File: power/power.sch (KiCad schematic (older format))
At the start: 83 parts, among them J1 Conn_01x02_Female, J2 Conn_01x02_Female, J3 CONN_02X03, J4 Conn_01x06_Female, Q1 BS170, Q10 BS170, Q11 BS170, Q12 BSB014N04LX3, Q2 BS170, Q3 BS170, Q4 BS170, Q5 BS170, Q6 BS170, Q7 BS170, Q8 BS170, Q9 BS170, U1 MAX1648, U2 TPS2592xx, U3 LMC6482

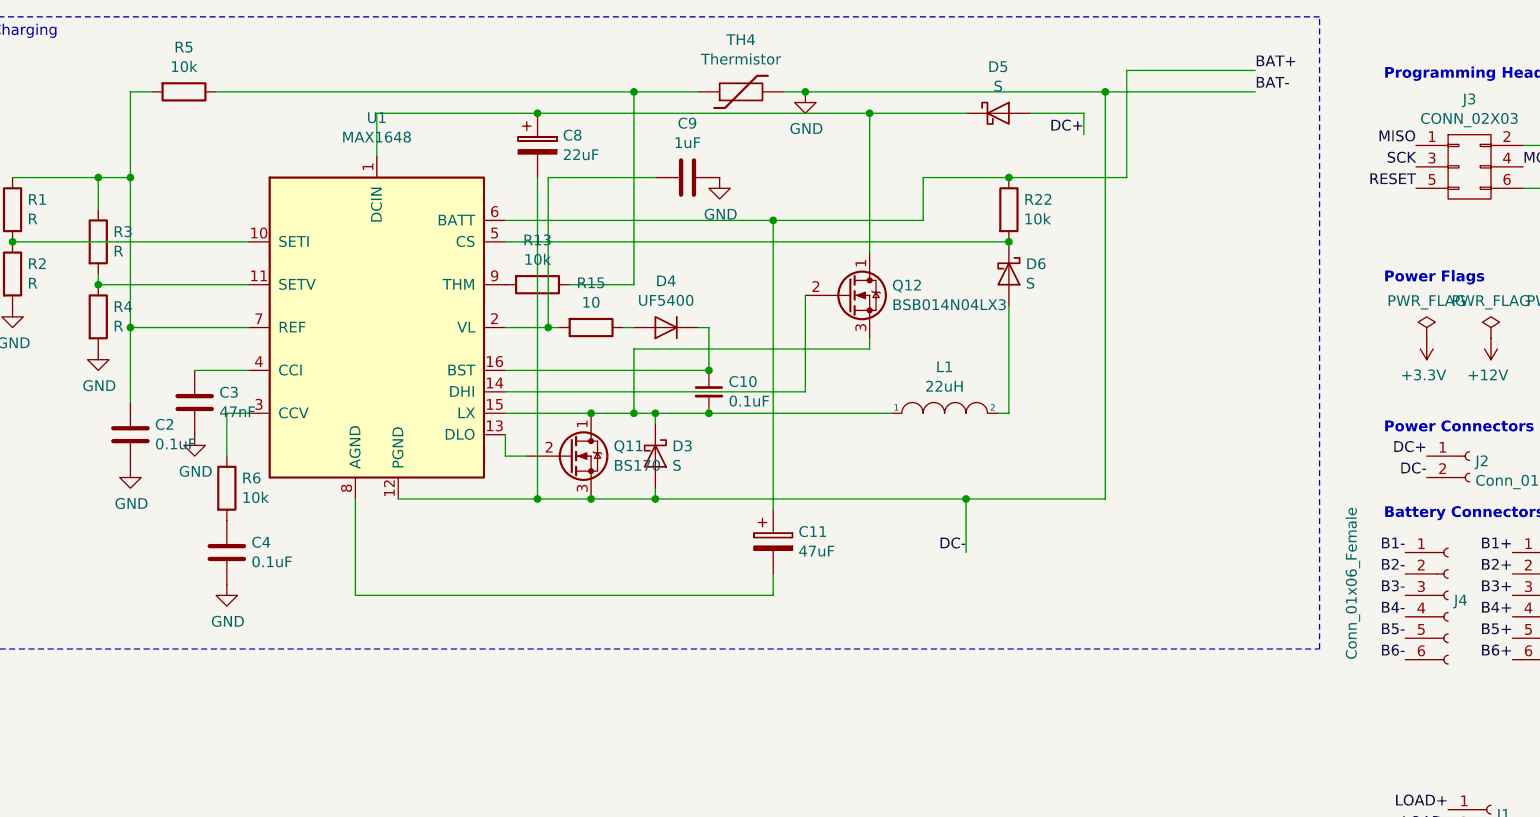
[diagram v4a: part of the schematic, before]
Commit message: wattage and values for charging circuit
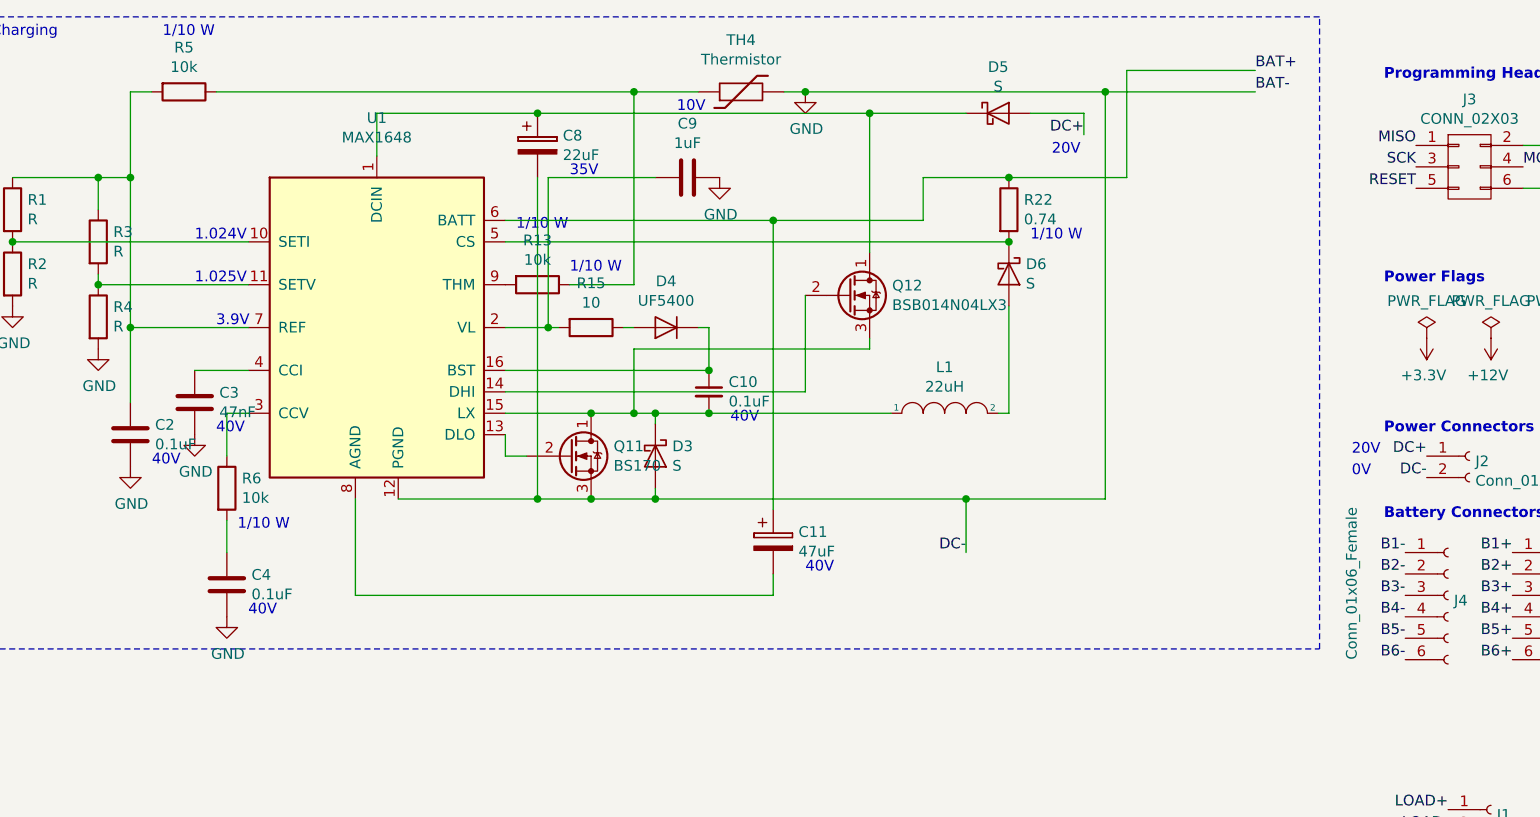
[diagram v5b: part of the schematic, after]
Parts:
- R22: value 10k -> 0.74
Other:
- note added: "0V"
- note added: "1.024V"
- note added: "1.025V"
- note added: "1/10 W"
- note added: "10V"
- note added: "20V"
- note added: "3.9V"
- note added: "35V"
- note added: "40V"
- moved on the sheet: C4
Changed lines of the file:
@@
 P 5300 1400
 F 0 "R22" H 5370 1446 50  0000 L CNN
-F 1 "10k" H 5370 1355 50  0000 L CNN
+F 1 "0.74" H 5370 1355 50  0000 L CNN
 F 2 "Resistor_SMD:R_0805_2012Metric_Pad1.15x1.40mm_HandSolder" V 5230 1400 50  0001 C CNN
 F 3 "~" H 5300 1400 50  0001 C CNN
@@
 L Device:C C4
 U 1 1 5E57A175
-P 1650 3000
-F 0 "C4" H 1535 2954 50  0000 R CNN
-F 1 "0.1uF" H 1535 3045 50  0000 R CNN
-F 2 "Capacitor_SMD:C_0805_2012Metric_Pad1.15x1.40mm_HandSolder" H 1688 2850 50  0001 C CNN
-F 3 "~" H 1650 3000 50  0001 C CNN
-	1    1650 3000
+P 1650 3150
+F 0 "C4" H 1535 3104 50  0000 R CNN
+F 1 "0.1uF" H 1535 3195 50  0000 R CNN
+F 2 "Capacitor_SMD:C_0805_2012Metric_Pad1.15x1.40mm_HandSolder" H 1688 3000 50  0001 C CNN
+F 3 "~" H 1650 3150 50  0001 C CNN
+	1    1650 3150
 	-1   0    0    1
 $EndComp
@@
 L power:GND #PWR0111
 U 1 1 5E588124
-P 1650 3150
-F 0 "#PWR0111" H 1650 2900 50  0001 C CNN
-F 1 "GND" H 1655 2977 50  0000 C CNN
-F 2 "" H 1650 3150 50  0001 C CNN
-F 3 "" H 1650 3150 50  0001 C CNN
-	1    1650 3150
+P 1650 3300
+F 0 "#PWR0111" H 1650 3050 50  0001 C CNN
+F 1 "GND" H 1655 3127 50  0000 C CNN
+F 2 "" H 1650 3300 50  0001 C CNN
+F 3 "" H 1650 3300 50  0001 C CNN
+	1    1650 3300
 	1    0    0    -1
 $EndComp
@@
 Text Label 10600 2500 0    50   ~ 0
 SafetySwitchB
+Text Notes 1700 2900 0    50   ~ 0
+1/10 W
+Wire Wire Line
+	1650 2850 1650 3000
+Text Notes 1750 3300 0    50   ~ 0
+40V
+Text Notes 1350 600  0    50   ~ 0
+1/10 W
+Text Notes 3000 1500 0    50   ~ 0
+1/10 W
+Text Notes 3250 1700 0    50   ~ 0
+1/10 W
+Text Notes 4350 3100 0    50   ~ 0
+40V
+Text Notes 4000 2400 0    50   ~ 0
+40V
+Text Notes 3250 1250 0    50   ~ 0
+35V
+Text Notes 3750 950  0    50   ~ 0
+10V
+Text Notes 1300 2600 0    50   ~ 0
+40V
+Text Notes 1600 2450 0    50   ~ 0
+40V
+Text Notes 5500 1150 0    50   ~ 0
+20V
+Text Notes 6900 2550 0    50   ~ 0
+20V
+Text Notes 6900 2650 0    50   ~ 0
+0V
+Text Notes 1600 1950 0    50   ~ 0
+3.9V
+Text Notes 1500 1550 0    50   ~ 0
+1.024V
+Text Notes 5400 1550 0    50   ~ 0
+1/10 W
+Text Notes 1500 1750 0    50   ~ 0
+1.025V
 $EndSCHEMATC

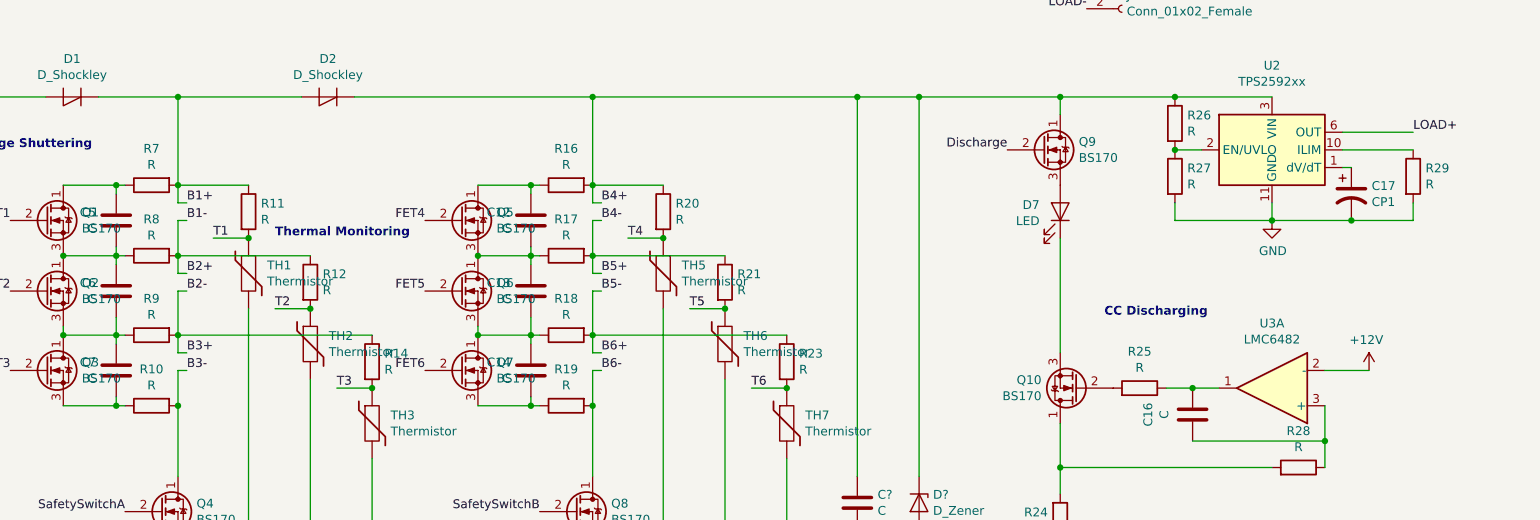
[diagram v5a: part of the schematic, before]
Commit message: bleeding resistor values and wattage, discharging current sink circuit complete
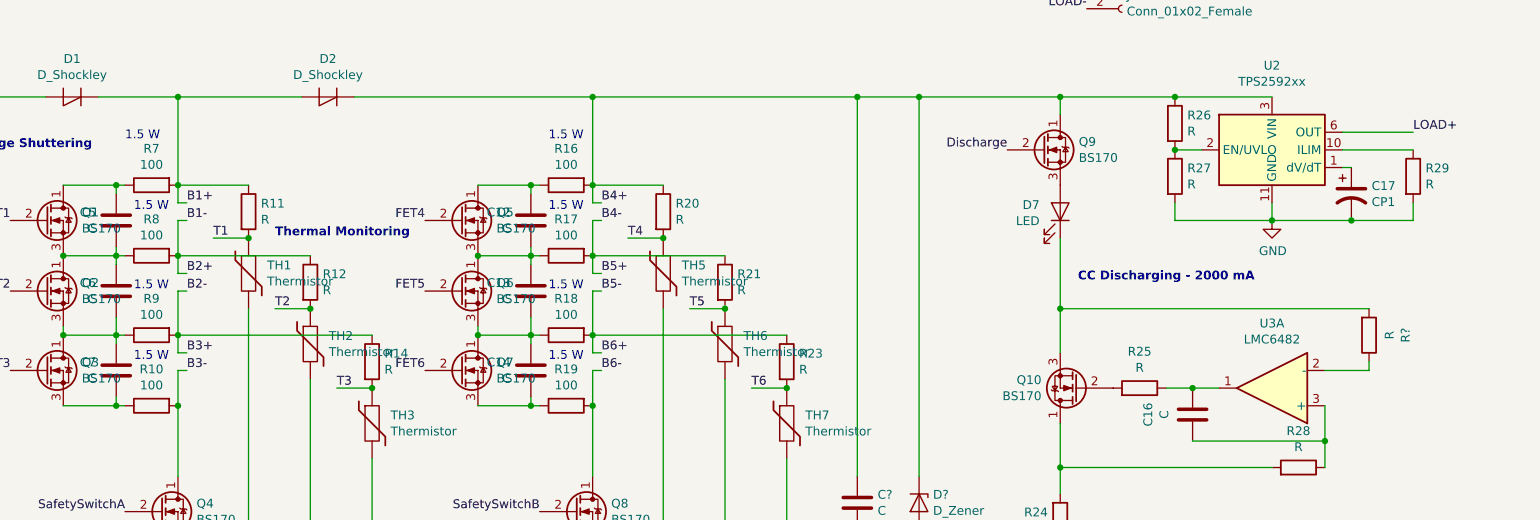
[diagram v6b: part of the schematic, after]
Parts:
- added R?: R, Resistor_SMD:R_0805_2012Metric_Pad1.15x1.40mm_HandSolder, symbol Device:R
- R10, R16, R17, R18, R19, R7, R8, R9: value R -> 100
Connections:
- net +12V: no longer U3.2 (-)
- net at D7.1 (K), Q10.3 (S): now also R?.2
- new net: R?.1, U3.2 (-)
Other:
- note added: "1.5 W"
- note added: "CC Discharging - 2000 mA"
- note removed: "CC Discharging"
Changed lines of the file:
@@
 Comment4 ""
 $EndDescr
-Text Notes 7450 6050 0    50   ~ 10
-CC Discharging
+Text Notes 7300 5850 0    50   ~ 10
+CC Discharging - 2000 mA
 $Comp
 L Device:LED D7
@@
 P 2050 5300
 F 0 "R7" V 1843 5300 50  0000 C CNN
-F 1 "R" V 1934 5300 50  0000 C CNN
+F 1 "100" V 1934 5300 50  0000 C CNN
 F 2 "Resistor_SMD:R_0805_2012Metric_Pad1.15x1.40mm_HandSolder" V 1980 5300 50  0001 C CNN
 F 3 "~" H 2050 5300 50  0001 C CNN
@@
 P 2050 5700
 F 0 "R8" V 1843 5700 50  0000 C CNN
-F 1 "R" V 1934 5700 50  0000 C CNN
+F 1 "100" V 1934 5700 50  0000 C CNN
 F 2 "Resistor_SMD:R_0805_2012Metric_Pad1.15x1.40mm_HandSolder" V 1980 5700 50  0001 C CNN
 F 3 "~" H 2050 5700 50  0001 C CNN
@@
 P 2050 6150
 F 0 "R9" V 1843 6150 50  0000 C CNN
-F 1 "R" V 1934 6150 50  0000 C CNN
+F 1 "100" V 1934 6150 50  0000 C CNN
 F 2 "Resistor_SMD:R_0805_2012Metric_Pad1.15x1.40mm_HandSolder" V 1980 6150 50  0001 C CNN
 F 3 "~" H 2050 6150 50  0001 C CNN
@@
 P 2050 6550
 F 0 "R10" V 1843 6550 50  0000 C CNN
-F 1 "R" V 1934 6550 50  0000 C CNN
+F 1 "100" V 1934 6550 50  0000 C CNN
 F 2 "Resistor_SMD:R_0805_2012Metric_Pad1.15x1.40mm_HandSolder" V 1980 6550 50  0001 C CNN
 F 3 "~" H 2050 6550 50  0001 C CNN
@@
 	1    0    0    -1
 $EndComp
-$Comp
-L power:+12V #PWR0106
-U 1 1 5E166418
-P 8950 6350
-F 0 "#PWR0106" H 8950 6200 50  0001 C CNN
-F 1 "+12V" H 8965 6523 50  0000 C CNN
-F 2 "" H 8950 6350 50  0001 C CNN
-F 3 "" H 8950 6350 50  0001 C CNN
-	1    8950 6350
-	-1   0    0    -1
-$EndComp
 Wire Wire Line
 	8950 6350 8700 6350
@@
 P 4400 5300
 F 0 "R16" V 4193 5300 50  0000 C CNN
-F 1 "R" V 4284 5300 50  0000 C CNN
+F 1 "100" V 4284 5300 50  0000 C CNN
 F 2 "Resistor_SMD:R_0805_2012Metric_Pad1.15x1.40mm_HandSolder" V 4330 5300 50  0001 C CNN
 F 3 "~" H 4400 5300 50  0001 C CNN
@@
 P 4400 5700
 F 0 "R17" V 4193 5700 50  0000 C CNN
-F 1 "R" V 4284 5700 50  0000 C CNN
+F 1 "100" V 4284 5700 50  0000 C CNN
 F 2 "Resistor_SMD:R_0805_2012Metric_Pad1.15x1.40mm_HandSolder" V 4330 5700 50  0001 C CNN
 F 3 "~" H 4400 5700 50  0001 C CNN
@@
 P 4400 6150
 F 0 "R18" V 4193 6150 50  0000 C CNN
-F 1 "R" V 4284 6150 50  0000 C CNN
+F 1 "100" V 4284 6150 50  0000 C CNN
 F 2 "Resistor_SMD:R_0805_2012Metric_Pad1.15x1.40mm_HandSolder" V 4330 6150 50  0001 C CNN
 F 3 "~" H 4400 6150 50  0001 C CNN
@@
 P 4400 6550
 F 0 "R19" V 4193 6550 50  0000 C CNN
-F 1 "R" V 4284 6550 50  0000 C CNN
+F 1 "100" V 4284 6550 50  0000 C CNN
 F 2 "Resistor_SMD:R_0805_2012Metric_Pad1.15x1.40mm_HandSolder" V 4330 6550 50  0001 C CNN
 F 3 "~" H 4400 6550 50  0001 C CNN
@@
 	3200 4800 4550 4800
 Wire Wire Line
-	7200 5600 7200 6250
+	7200 5600 7200 6000
 Wire Wire Line
 	7200 7350 7200 7550
@@
 Text Notes 1500 1750 0    50   ~ 0
 1.025V
+Text Notes 1900 5050 0    50   ~ 0
+1.5 W
+Text Notes 1950 5450 0    50   ~ 0
+1.5 W
+Text Notes 1950 5900 0    50   ~ 0
+1.5 W
+Text Notes 1950 6300 0    50   ~ 0
+1.5 W
+Text Notes 4300 5050 0    50   ~ 0
+1.5 W
+Text Notes 4300 5450 0    50   ~ 0
+1.5 W
+Text Notes 4300 5900 0    50   ~ 0
+1.5 W
+Text Notes 4300 6300 0    50   ~ 0
+1.5 W
+Wire Wire Line
+	7200 6000 8950 6000
+Connection ~ 7200 6000
+Wire Wire Line
+	7200 6000 7200 6250
+$Comp
+L Device:R R?
+U 1 1 5FD37C22
+P 8950 6150
+F 0 "R?" V 9157 6150 50  0000 C CNN
+F 1 "R" V 9066 6150 50  0000 C CNN
+F 2 "Resistor_SMD:R_0805_2012Metric_Pad1.15x1.40mm_HandSolder" V 8880 6150 50  0001 C CNN
+F 3 "~" H 8950 6150 50  0001 C CNN
+	1    8950 6150
+	1    0    0    1
+$EndComp
+Wire Wire Line
+	8950 6300 8950 6350
 $EndSCHEMATC

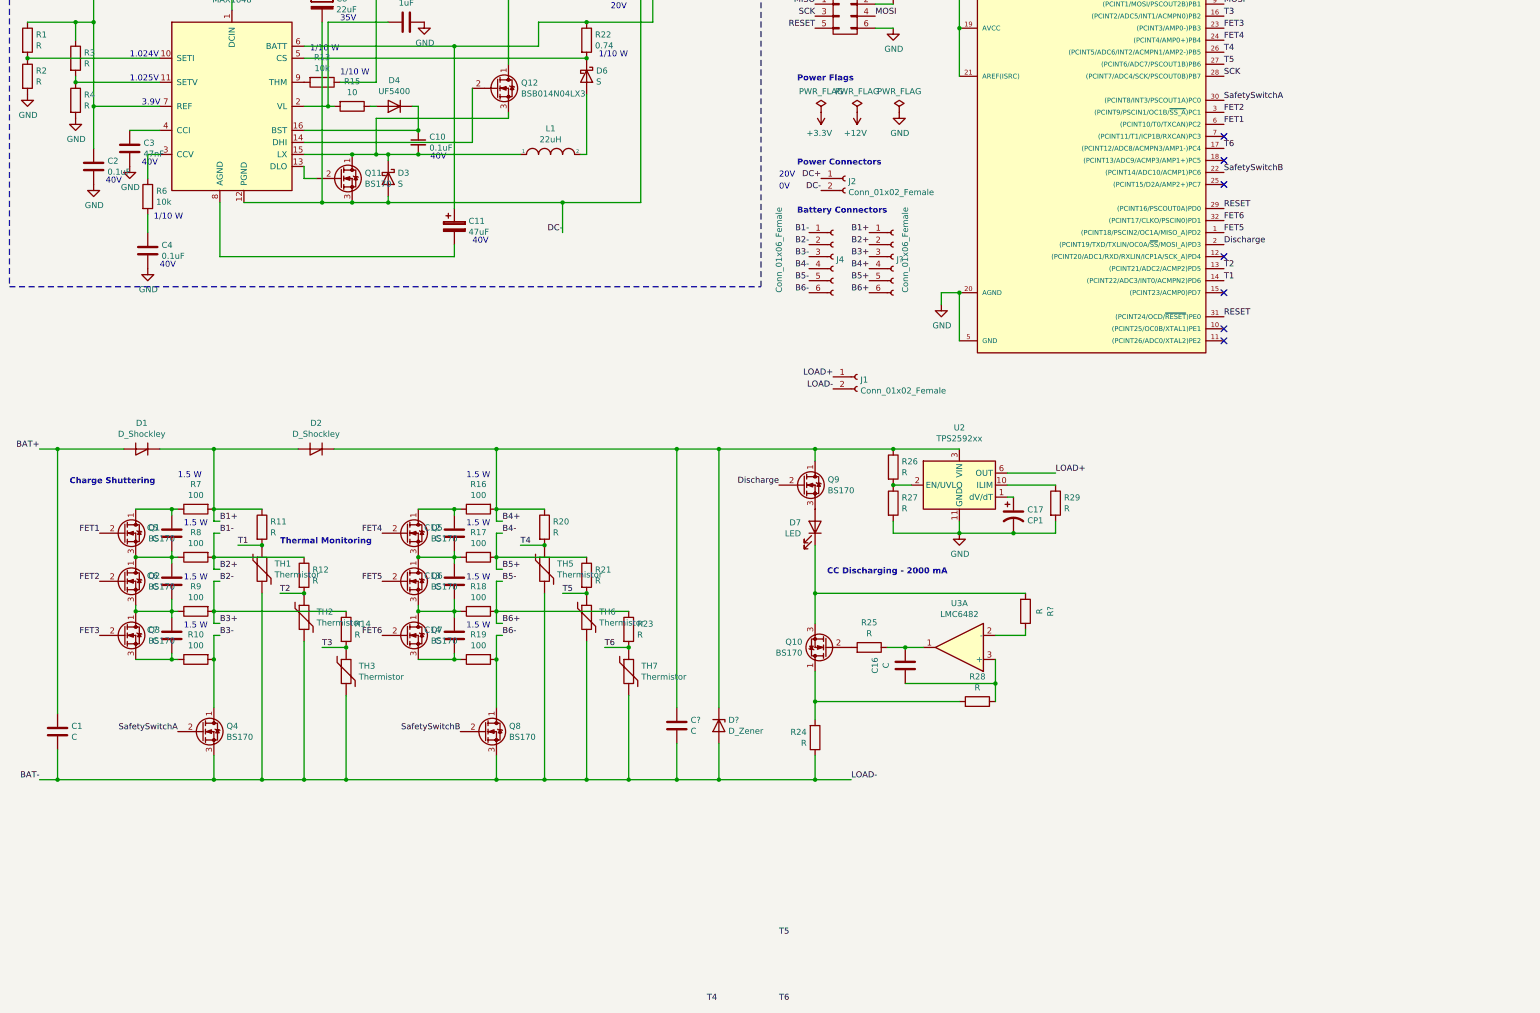
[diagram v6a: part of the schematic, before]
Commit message: buck converters added and LDO added
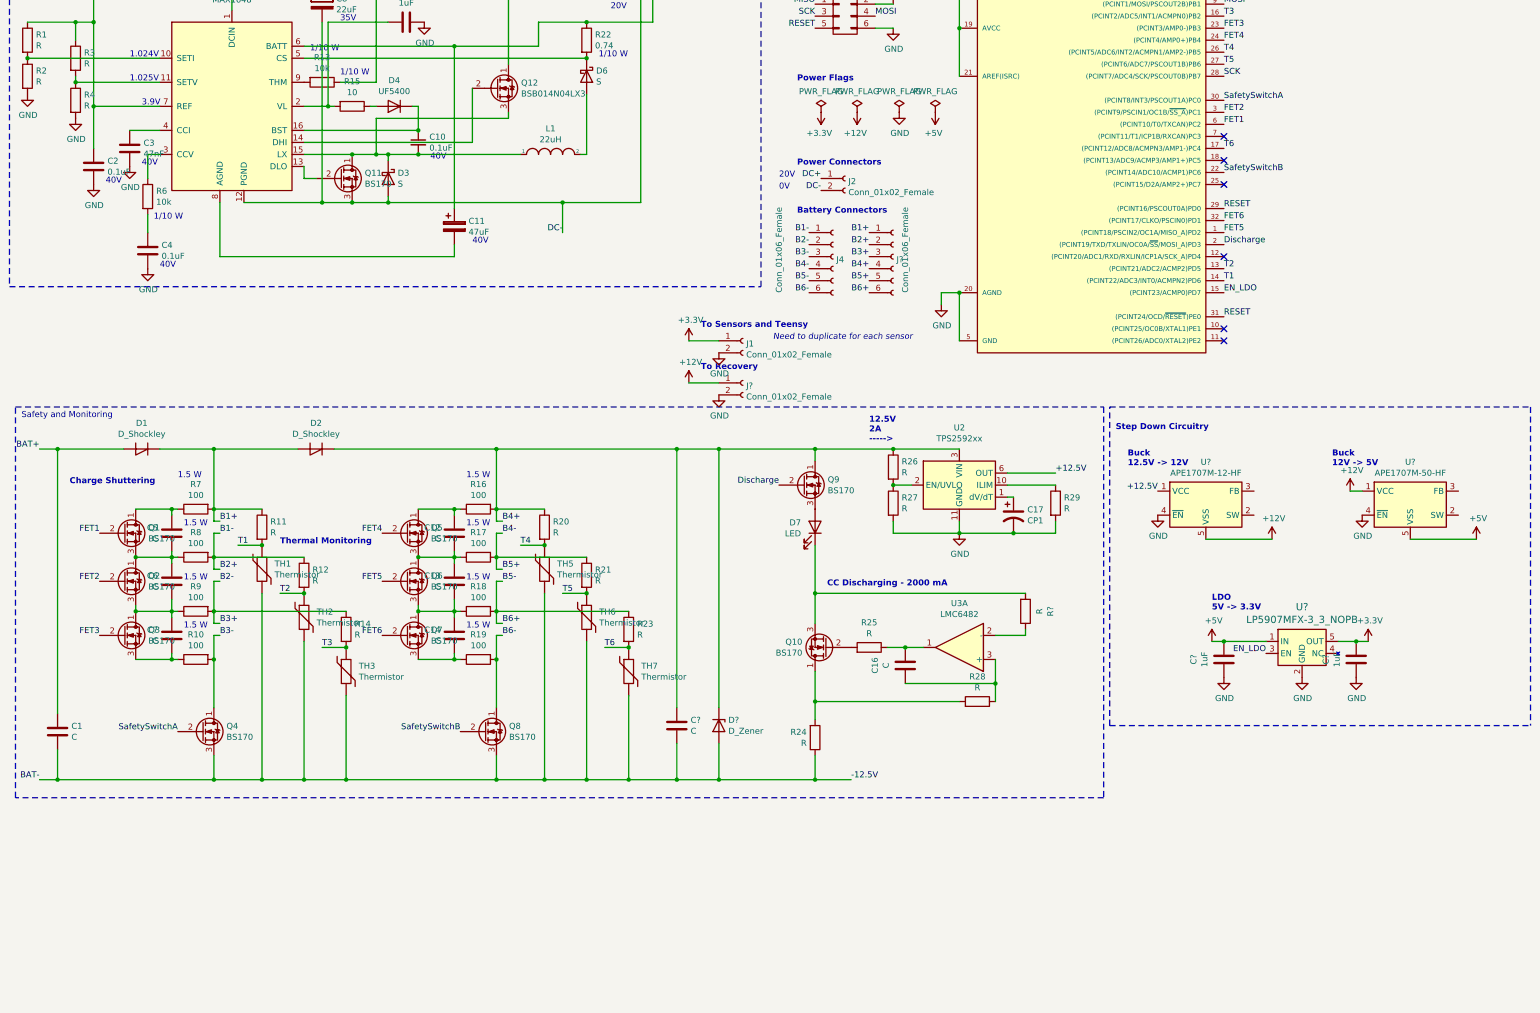
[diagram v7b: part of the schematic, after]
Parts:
- added C? (x2): 1uF, Capacitor_SMD:C_0805_2012Metric_Pad1.15x1.40mm_HandSolder, symbol Device:C
- added J?: Conn_01x02_Female, Connector_PinHeader_1.00mm:PinHeader_1x02_P1.00mm_Vertical, symbol Connector:Conn_01x02_Female
- added U?: LP5907MFX-3_3_NOPB, digikey-footprints:SOT-753, symbol dk_PMIC-Voltage-Regulators-Linear:LP5907MFX-3_3_NOPB
- added U?: APE1707M-12-HF, Package_SO:SOIC-8_3.9x4.9mm_P1.27mm, symbol Regulator_Switching:APE1707M-12-HF
- added U?: APE1707M-50-HF, Package_SO:SOIC-8_3.9x4.9mm_P1.27mm, symbol Regulator_Switching:APE1707M-50-HF
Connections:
- net +12V: now also J?.1 (Pin_1), U?.1 (VCC), U?.5 (VSS), U?.6 (VSS), U?.7 (VSS), U?.8 (VSS)
- net +3V3: now also J1.1 (Pin_1), C?.2, U?.5 (OUT)
- net GND: now also C?.1, C?.1, J?.2 (Pin_2), U?.2 (GND), U?.4 (~EN~), U?.4 (~EN~)
- net EN_LDO: now reaches U?.15 ((PCINT23/ACMP0)PD7)
- net EN_LDO: now also U?.3 (EN)
- net LOAD+ renamed +12.5V
- net +12.5V: now also U?.1 (VCC); no longer J1.1 (Pin_1)
- new net +5V: C?.2, U?.1 (IN), U?.5 (VSS), U?.6 (VSS), U?.7 (VSS), U?.8 (VSS)
- no-connect marks 7 -> 6
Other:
- note added: "12.5V \n2A\n----->"
- note added: "Buck\n12.5V -> 12V"
- note added: "Buck\n12V -> 5V"
- note added: "LDO\n5V -> 3.3V"
- note added: "Need to duplicate for each sensor"
- note added: "Safety and Monitoring\n"
- note added: "Step Down Circuitry"
- note added: "To Recovery"
- note added: "To Sensors and Teensy"
- moved on the sheet: J1
